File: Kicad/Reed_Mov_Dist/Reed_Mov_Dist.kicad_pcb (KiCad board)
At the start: 2 copper layers, 21 parts, among them J1 Barrel_Jack, J10 HC-SRO4, J11 URM37, J12 LV-MaxSonar-EZ1, J2 Conn_01x02, J3 Conn_01x02, J4 Conn_01x02, J5 LIS3DH_1, J6 ITG3200, J7 LIS3DH_2, J8 TTL_Level_Shifter_1, J9 TTL_Level_Shifter_2, U1 LM7805_TO220, U2 XBEE

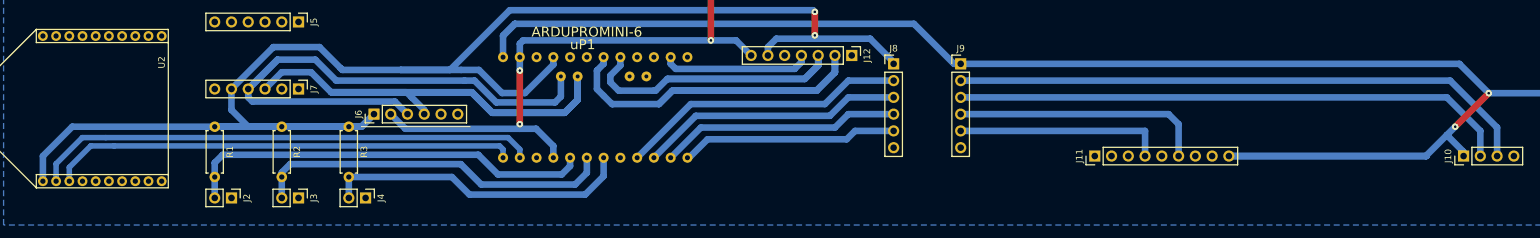
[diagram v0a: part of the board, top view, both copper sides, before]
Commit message: Corrected distance sensors bug. Added jumper to enable or disable Xbee, to access arduino pro mini serial port.
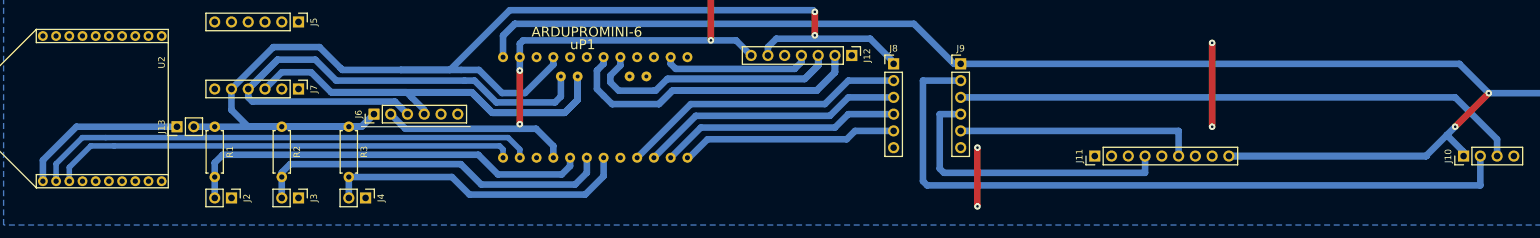
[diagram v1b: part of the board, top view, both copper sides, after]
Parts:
- added J13: Conn_01x02, Socket_Strips:Socket_Strip_Straight_1x02_Pitch2.54mm, F.Cu at (41.3, 78.1)
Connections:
- J9 pad 2: ECHO_HC_HV -> TRIG_HC_HV
- J9 pad 3: TRIG_HC_HV -> ECHO_HC_HV
- J9 pad 4: ECHO_URM_HV -> TRIG_URM_HV
- J9 pad 5: TRIG_URM_HV -> ECHO_URM_HV
- U2 pad 1: 3V3 -> 3V3_Xbee
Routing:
- net 3V3: track 238.7 -> 205.1 mm
- net 3V3_Xbee: track 0.00 -> 25.6 mm
- net TRIG_HC_HV: track 84.7 -> 110.1 mm
- net (no net): track 0.25 -> 21.8 mm, vias 0 -> 4
- net TRIG_URM_HV: track 31.8 -> 45.3 mm
- net ECHO_HC_HV: track 88.5 -> 86.5 mm
- net ECHO_URM_HV: track 38.5 -> 36.8 mm
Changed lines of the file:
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@@
 (kicad_pcb (version 4) (host pcbnew 4.0.7-e2-6376~58~ubuntu16.04.1)
   (general
-    (links 57)
-    (no_connects 0)
-    (area 14.924999 54.924999 280.075001 95.075001)
+    (links 58)
+    (no_connects 2)
+    (area 69.139999 78.029999 85.800001 78.180001)
     (thickness 1.6)
     (drawings 6)
-    (tracks 225)
+    (tracks 236)
     (zones 0)
-    (modules 21)
-    (nets 24)
+    (modules 22)
+    (nets 25)
   )
   (page A4)
@@
   (net 22 Rx)
   (net 23 Tx)
+  (net 24 3V3_Xbee)
   (net_class Default "This is the default net class."
     (clearance 0.42)
@@
     (uvia_drill 0.1)
     (add_net 3V3)
+    (add_net 3V3_Xbee)
     (add_net 5V)
     (add_net ADC_EZ1)
@@
       (net 1 5V))
     (pad 2 thru_hole oval (at 0 2.54) (size 1.7 1.7) (drill 1) (layers *.Cu *.Mask)
+      (net 15 TRIG_HC_HV))
+    (pad 3 thru_hole oval (at 0 5.08) (size 1.7 1.7) (drill 1) (layers *.Cu *.Mask)
       (net 16 ECHO_HC_HV))
-    (pad 3 thru_hole oval (at 0 5.08) (size 1.7 1.7) (drill 1) (layers *.Cu *.Mask)
-      (net 15 TRIG_HC_HV))
     (pad 4 thru_hole oval (at 0 7.62) (size 1.7 1.7) (drill 1) (layers *.Cu *.Mask)
+      (net 17 TRIG_URM_HV))
+    (pad 5 thru_hole oval (at 0 10.16) (size 1.7 1.7) (drill 1) (layers *.Cu *.Mask)
       (net 18 ECHO_URM_HV))
-    (pad 5 thru_hole oval (at 0 10.16) (size 1.7 1.7) (drill 1) (layers *.Cu *.Mask)
-      (net 17 TRIG_URM_HV))
     (pad 6 thru_hole oval (at 0 12.7) (size 1.7 1.7) (drill 1) (layers *.Cu *.Mask)
       (net 2 GND))
@@
     (fp_line (start 23 -1) (end 15 -9) (layer F.SilkS) (width 0.15))
     (pad 1 thru_hole circle (at 0 0 90) (size 1.5 1.5) (drill 0.8) (layers *.Cu *.Mask F.SilkS)
-      (net 8 3V3))
+      (net 24 3V3_Xbee))
     (pad 2 thru_hole circle (at 0 2 90) (size 1.5 1.5) (drill 0.8) (layers *.Cu *.Mask F.SilkS)
       (net 22 Rx))
@@
     )
   )
+  (module Socket_Strips:Socket_Strip_Straight_1x02_Pitch2.54mm (layer F.Cu)
+    (at 41.275 78.105 90)
+    (descr "Through hole straight socket strip, 1x02, 2.54mm pitch, single row")
+    (tags "Through hole socket strip THT 1x02 2.54mm single row")
+    (fp_text reference J13 (at 0 -2.33 90) (layer F.SilkS)
+      (effects (font (size 1 1) (thickness 0.15)))
+    )
+    (fp_text value Conn_01x02 (at 0 4.87 90) (layer F.Fab)
+      (effects (font (size 1 1) (thickness 0.15)))
+    )
+    (fp_line (start -1.27 -1.27) (end -1.27 3.81) (layer F.Fab) (width 0.1))
+    (fp_line (start -1.27 3.81) (end 1.27 3.81) (layer F.Fab) (width 0.1))
+    (fp_line (start 1.27 3.81) (end 1.27 -1.27) (layer F.Fab) (width 0.1))
+    (fp_line (start 1.27 -1.27) (end -1.27 -1.27) (layer F.Fab) (width 0.1))
+    (fp_line (start -1.33 1.27) (end -1.33 3.87) (layer F.SilkS) (width 0.12))
+    (fp_line (start -1.33 3.87) (end 1.33 3.87) (layer F.SilkS) (width 0.12))
+    (fp_line (start 1.33 3.87) (end 1.33 1.27) (layer F.SilkS) (width 0.12))
+    (fp_line (start 1.33 1.27) (end -1.33 1.27) (layer F.SilkS) (width 0.12))
+    (fp_line (start -1.33 0) (end -1.33 -1.33) (layer F.SilkS) (width 0.12))
+    (fp_line (start -1.33 -1.33) (end 0 -1.33) (layer F.SilkS) (width 0.12))
+    (fp_line (start -1.8 -1.8) (end -1.8 4.35) (layer F.CrtYd) (width 0.05))
+    (fp_line (start -1.8 4.35) (end 1.8 4.35) (layer F.CrtYd) (width 0.05))
+    (fp_line (start 1.8 4.35) (end 1.8 -1.8) (layer F.CrtYd) (width 0.05))
+    (fp_line (start 1.8 -1.8) (end -1.8 -1.8) (layer F.CrtYd) (width 0.05))
+    (fp_text user %R (at 0 -2.33 90) (layer F.Fab)
+      (effects (font (size 1 1) (thickness 0.15)))
+    )
+    (pad 1 thru_hole rect (at 0 0 90) (size 1.7 1.7) (drill 1) (layers *.Cu *.Mask)
+      (net 24 3V3_Xbee))
+    (pad 2 thru_hole oval (at 0 2.54 90) (size 1.7 1.7) (drill 1) (layers *.Cu *.Mask)
+      (net 8 3V3))
+    (model ${KISYS3DMOD}/Socket_Strips.3dshapes/Socket_Strip_Straight_1x02_Pitch2.54mm.wrl
+      (at (xyz 0 -0.05 0))
+      (scale (xyz 1 1 1))
+      (rotate (xyz 0 0 270))
+    )
+  )
   (gr_line (start 280 93) (end 15 93) (angle 90) (layer Margin) (width 0.2))
   (gr_line (start 15 57) (end 280 57) (angle 90) (layer Margin) (width 0.2))
@@
   (gr_line (start 69.215 78.105) (end 85.725 78.105) (angle 90) (layer Edge.Cuts) (width 0.15))
   (segment (start 113.538 67.564) (end 113.538 67.818) (width 1) (layer B.Cu) (net 0))
+  (via (at 198.12 78.105) (size 1) (drill 0.4) (layers F.Cu B.Cu) (net 0))
+  (via (at 198.12 65.405) (size 1) (drill 0.4) (layers F.Cu B.Cu) (net 0))
+  (segment (start 198.12 78.105) (end 198.12 65.405) (width 1) (layer F.Cu) (net 0))
+  (via (at 162.56 81.28) (size 1) (drill 0.4) (layers F.Cu B.Cu) (net 0))
+  (via (at 162.56 90.17) (size 1) (drill 0.4) (layers F.Cu B.Cu) (net 0))
+  (segment (start 162.56 81.28) (end 162.56 90.17) (width 1) (layer F.Cu) (net 0))
   (segment (start 270.764 75.692) (end 270.764 76.581) (width 1) (layer B.Cu) (net 1))
   (segment (start 270.764 76.581) (end 266.7 80.645) (width 1) (layer B.Cu) (net 1))
@@
   (segment (start 230.505 82.55) (end 233.68 79.375) (width 1) (layer B.Cu) (net 1))
   (segment (start 233.68 79.375) (end 234.95 78.105) (width 1) (layer B.Cu) (net 1))
-  (via (at 240.03 73.025) (size 1) (drill 0.4) (layers F.Cu B.Cu) (net 1) (status 1000000))
+  (via (at 240.03 73.025) (size 1) (drill 0.4) (layers F.Cu B.Cu) (net 1))
   (segment (start 234.95 78.105) (end 240.03 73.025) (width 1) (layer F.Cu) (net 1))
   (via (at 234.95 78.105) (size 1) (drill 0.4) (layers F.Cu B.Cu) (net 1))
@@
   (segment (start 82.931 85.725) (end 85.598 88.392) (width 1) (layer B.Cu) (net 7))
   (segment (start 67.31 85.725) (end 67.31 88.9) (width 1) (layer B.Cu) (net 7))
+  (segment (start 43.815 78.105) (end 46.99 78.105) (width 1) (layer B.Cu) (net 8) (status C00000))
   (segment (start 67.31 78.105) (end 69.215 78.105) (width 1) (layer B.Cu) (net 8))
   (segment (start 69.215 78.105) (end 71.12 76.2) (width 1) (layer B.Cu) (net 8))
@@
   (segment (start 49.53 72.39) (end 49.53 75.565) (width 1) (layer B.Cu) (net 8))
   (segment (start 49.53 75.565) (end 52.07 78.105) (width 1) (layer B.Cu) (net 8))
-  (segment (start 25.4 78.105) (end 52.07 78.105) (width 1) (layer B.Cu) (net 8))
   (segment (start 52.07 78.105) (end 69.215 78.105) (width 1) (layer B.Cu) (net 8))
   (segment (start 69.215 78.105) (end 71.12 76.2) (width 1) (layer B.Cu) (net 8))
-  (segment (start 20.955 82.55) (end 20.955 86.36) (width 1) (layer B.Cu) (net 8))
-  (segment (start 25.4 78.105) (end 20.955 82.55) (width 1) (layer B.Cu) (net 8))
   (segment (start 75.184 69.5025) (end 82.6435 69.5025) (width 1) (layer B.Cu) (net 8))
   (segment (start 137.922 64.262) (end 137.922 64.77) (width 1) (layer B.Cu) (net 8))
@@
   (segment (start 142.748 80.01) (end 144.018 78.74) (width 1) (layer B.Cu) (net 14))
   (segment (start 144.018 78.74) (end 149.86 78.74) (width 1) (layer B.Cu) (net 14))
-  (segment (start 238.76 82.55) (end 238.76 78.74) (width 1) (layer B.Cu) (net 15))
-  (segment (start 233.68 73.66) (end 160.02 73.66) (width 1) (layer B.Cu) (net 15))
-  (segment (start 238.76 78.74) (end 233.68 73.66) (width 1) (layer B.Cu) (net 15))
-  (segment (start 241.3 82.55) (end 241.3 78.232) (width 1) (layer B.Cu) (net 16))
-  (segment (start 234.188 71.12) (end 160.02 71.12) (width 1) (layer B.Cu) (net 16))
-  (segment (start 241.3 78.232) (end 234.188 71.12) (width 1) (layer B.Cu) (net 16))
-  (segment (start 187.96 82.55) (end 187.96 78.74) (width 1) (layer B.Cu) (net 17))
-  (segment (start 187.96 78.74) (end 160.02 78.74) (width 1) (layer B.Cu) (net 17))
-  (segment (start 193.04 82.55) (end 193.04 77.724) (width 1) (layer B.Cu) (net 18))
-  (segment (start 191.516 76.2) (end 160.02 76.2) (width 1) (layer B.Cu) (net 18))
-  (segment (start 193.04 77.724) (end 191.516 76.2) (width 1) (layer B.Cu) (net 18))
+  (segment (start 160.02 71.12) (end 154.305 71.12) (width 1) (layer B.Cu) (net 15))
+  (segment (start 238.76 86.995) (end 238.76 82.55) (width 1) (layer B.Cu) (net 15))
+  (segment (start 154.94 86.995) (end 238.76 86.995) (width 1) (layer B.Cu) (net 15))
+  (segment (start 154.305 86.36) (end 154.94 86.995) (width 1) (layer B.Cu) (net 15))
+  (segment (start 154.305 71.12) (end 154.305 86.36) (width 1) (layer B.Cu) (net 15))
+  (segment (start 241.3 82.55) (end 241.3 80.01) (width 1) (layer B.Cu) (net 16))
+  (segment (start 234.95 73.66) (end 160.02 73.66) (width 1) (layer B.Cu) (net 16))
+  (segment (start 241.3 80.01) (end 234.95 73.66) (width 1) (layer B.Cu) (net 16))
+  (segment (start 160.02 76.2) (end 156.845 76.2) (width 1) (layer B.Cu) (net 17))
+  (segment (start 187.96 85.09) (end 187.96 82.55) (width 1) (layer B.Cu) (net 17))
+  (segment (start 157.48 85.09) (end 187.96 85.09) (width 1) (layer B.Cu) (net 17))
+  (segment (start 156.845 84.455) (end 157.48 85.09) (width 1) (layer B.Cu) (net 17))
+  (segment (start 156.845 76.2) (end 156.845 84.455) (width 1) (layer B.Cu) (net 17))
+  (segment (start 160.02 78.74) (end 193.04 78.74) (width 1) (layer B.Cu) (net 18))
+  (segment (start 193.04 78.74) (end 193.04 82.55) (width 1) (layer B.Cu) (net 18))
   (segment (start 107.315 74.676) (end 114.3 74.676) (width 1) (layer B.Cu) (net 19))
   (segment (start 114.3 74.676) (end 116.332 72.644) (width 1) (layer B.Cu) (net 19))
@@
   (segment (start 90.160002 81.016002) (end 90.678 81.534) (width 0.84) (layer B.Cu) (net 23))
   (segment (start 31.75 81.016002) (end 90.160002 81.016002) (width 0.84) (layer B.Cu) (net 23))
+  (segment (start 41.275 78.105) (end 26.035 78.105) (width 1) (layer B.Cu) (net 24) (status 400000))
+  (segment (start 20.955 83.185) (end 20.955 86.36) (width 1) (layer B.Cu) (net 24) (status 800000))
+  (segment (start 26.035 78.105) (end 20.955 83.185) (width 1) (layer B.Cu) (net 24))
   (zone (net 2) (net_name GND) (layer B.Cu) (hatch edge 0.508)
     (priority 100)
